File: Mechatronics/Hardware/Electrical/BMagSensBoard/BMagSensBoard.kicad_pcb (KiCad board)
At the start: 2 copper layers, 20 x 17.6 mm, 2 parts, among them J1 Conn_01x06_Male, U1 TLE5009

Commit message: Changes
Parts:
- added C27: 100nF, Encoder:C_0603_1608Metric_Pad1.05x0.95mm_HandSolder, F.Cu at (147.3, 83.7)
- renumbered J1 to J7, U1 to U7
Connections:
- net /GND renamed GND
- U7 pad 8: Net-(U1-Pad8) -> (no net)
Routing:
- net /VDD: track 9.26 -> 18.7 mm
- net /COS_P: track 10.3 -> 13.1 mm
- net GND: track 5.48 -> 6.84 mm, vias 0 -> 3
- net /COS_N: track 8.87 -> 9.61 mm
- added copper zone on F.Cu, net GND
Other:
- board size 20 x 17.6 mm -> 20 x 18.1 mm

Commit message: Changed files
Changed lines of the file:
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@@
   )
   (setup
-    (last_trace_width 0.635)
+    (last_trace_width 0.127)
     (user_trace_width 0.127)
     (user_trace_width 0.254)
@@
     (add_net GND)
   )
+  (module Encoder:SO-8_3.9x4.9mm_P1.27mm (layer F.Cu)
+    (at 146.812 88.4428)
+    (descr "SO, 8 Pin (https://www.nxp.com/docs/en/data-sheet/PCF8523.pdf), generated with kicad-footprint-generator ipc_gullwing_generator.py")
+    (tags "SO SO")
+    (attr smd)
+    (fp_text reference U7 (at -3.048 -3.4) (layer F.SilkS)
+      (effects (font (size 1 1) (thickness 0.15)))
+    )
+    (fp_text value TLE5009 (at 0 3.4) (layer F.Fab)
+      (effects (font (size 1 1) (thickness 0.15)))
+    )
+    (fp_text user %R (at 0 0) (layer F.Fab)
+      (effects (font (size 0.98 0.98) (thickness 0.15)))
+    )
+    (fp_line (start 3.7 -2.7) (end -3.7 -2.7) (layer F.CrtYd) (width 0.05))
+    (fp_line (start 3.7 2.7) (end 3.7 -2.7) (layer F.CrtYd) (width 0.05))
+    (fp_line (start -3.7 2.7) (end 3.7 2.7) (layer F.CrtYd) (width 0.05))
+    (fp_line (start -3.7 -2.7) (end -3.7 2.7) (layer F.CrtYd) (width 0.05))
+    (fp_line (start -1.95 -1.475) (end -0.975 -2.45) (layer F.Fab) (width 0.1))
+    (fp_line (start -1.95 2.45) (end -1.95 -1.475) (layer F.Fab) (width 0.1))
+    (fp_line (start 1.95 2.45) (end -1.95 2.45) (layer F.Fab) (width 0.1))
+    (fp_line (start 1.95 -2.45) (end 1.95 2.45) (layer F.Fab) (width 0.1))
+    (fp_line (start -0.975 -2.45) (end 1.95 -2.45) (layer F.Fab) (width 0.1))
+    (fp_line (start 0 -2.56) (end -3.45 -2.56) (layer F.SilkS) (width 0.12))
+    (fp_line (start 0 -2.56) (end 1.95 -2.56) (layer F.SilkS) (width 0.12))
+    (fp_line (start 0 2.56) (end -1.95 2.56) (layer F.SilkS) (width 0.12))
+    (fp_line (start 0 2.56) (end 1.95 2.56) (layer F.SilkS) (width 0.12))
+    (pad 1 smd roundrect (at -2.845 -1.905) (size 1.31 0.65) (layers F.Cu F.Paste F.Mask) (roundrect_rratio 0.25)
+      (net 3 /COS_P))
+    (pad 2 smd roundrect (at -2.845 -0.635) (size 1.31 0.6) (layers F.Cu F.Paste F.Mask) (roundrect_rratio 0.25)
+      (net 2 /COS_N))
+    (pad 3 smd roundrect (at -2.845 0.635) (size 1.31 0.6) (layers F.Cu F.Paste F.Mask) (roundrect_rratio 0.25)
+      (net 6 GND))
+    (pad 4 smd roundrect (at -2.845 1.905) (size 1.31 0.6) (layers F.Cu F.Paste F.Mask) (roundrect_rratio 0.25)
+      (net 6 GND))
+    (pad 5 smd roundrect (at 2.845 1.905) (size 1.31 0.6) (layers F.Cu F.Paste F.Mask) (roundrect_rratio 0.25)
+      (net 1 /SIN_P))
+    (pad 6 smd roundrect (at 2.845 0.635) (size 1.31 0.6) (layers F.Cu F.Paste F.Mask) (roundrect_rratio 0.25)
+      (net 5 /SIN_N))
+    (pad 7 smd roundrect (at 2.845 -0.635) (size 1.31 0.6) (layers F.Cu F.Paste F.Mask) (roundrect_rratio 0.25)
+      (net 4 /VDD))
+    (pad 8 smd roundrect (at 2.84 -1.905) (size 1.31 0.6) (layers F.Cu F.Paste F.Mask) (roundrect_rratio 0.25))
+    (model "${KIPRJMOD}/../FootPrints/3DModels/So8/User Library-so8-3.step"
+      (at (xyz 0 0 0))
+      (scale (xyz 1 1 1))
+      (rotate (xyz 0 0 0))
+    )
+  )
   (module Encoder:SolderWirePad_1x01_SMD_5x10mm (layer F.Cu)
     (at 146.812 93.7768)
@@
       (net 2 /COS_N))
   )
-  (module Encoder:SO-8_3.9x4.9mm_P1.27mm (layer F.Cu)
-    (at 146.812 88.4428)
-    (descr "SO, 8 Pin (https://www.nxp.com/docs/en/data-sheet/PCF8523.pdf), generated with kicad-footprint-generator ipc_gullwing_generator.py")
-    (tags "SO SO")
-    (attr smd)
-    (fp_text reference U7 (at -3.048 -3.4) (layer F.SilkS)
-      (effects (font (size 1 1) (thickness 0.15)))
-    )
-    (fp_text value TLE5009 (at 0 3.4) (layer F.Fab)
-      (effects (font (size 1 1) (thickness 0.15)))
-    )
-    (fp_line (start 3.7 -2.7) (end -3.7 -2.7) (layer F.CrtYd) (width 0.05))
-    (fp_line (start 3.7 2.7) (end 3.7 -2.7) (layer F.CrtYd) (width 0.05))
-    (fp_line (start -3.7 2.7) (end 3.7 2.7) (layer F.CrtYd) (width 0.05))
-    (fp_line (start -3.7 -2.7) (end -3.7 2.7) (layer F.CrtYd) (width 0.05))
-    (fp_line (start -1.95 -1.475) (end -0.975 -2.45) (layer F.Fab) (width 0.1))
-    (fp_line (start -1.95 2.45) (end -1.95 -1.475) (layer F.Fab) (width 0.1))
-    (fp_line (start 1.95 2.45) (end -1.95 2.45) (layer F.Fab) (width 0.1))
-    (fp_line (start 1.95 -2.45) (end 1.95 2.45) (layer F.Fab) (width 0.1))
-    (fp_line (start -0.975 -2.45) (end 1.95 -2.45) (layer F.Fab) (width 0.1))
-    (fp_line (start 0 -2.56) (end -3.45 -2.56) (layer F.SilkS) (width 0.12))
-    (fp_line (start 0 -2.56) (end 1.95 -2.56) (layer F.SilkS) (width 0.12))
-    (fp_line (start 0 2.56) (end -1.95 2.56) (layer F.SilkS) (width 0.12))
-    (fp_line (start 0 2.56) (end 1.95 2.56) (layer F.SilkS) (width 0.12))
-    (fp_text user %R (at 0 0) (layer F.Fab)
-      (effects (font (size 0.98 0.98) (thickness 0.15)))
-    )
-    (pad 1 smd roundrect (at -2.575 -1.905) (size 1.75 0.6) (layers F.Cu F.Paste F.Mask) (roundrect_rratio 0.25)
-      (net 3 /COS_P))
-    (pad 2 smd roundrect (at -2.575 -0.635) (size 1.75 0.6) (layers F.Cu F.Paste F.Mask) (roundrect_rratio 0.25)
-      (net 2 /COS_N))
-    (pad 3 smd roundrect (at -2.575 0.635) (size 1.75 0.6) (layers F.Cu F.Paste F.Mask) (roundrect_rratio 0.25)
-      (net 6 GND))
-    (pad 4 smd roundrect (at -2.575 1.905) (size 1.75 0.6) (layers F.Cu F.Paste F.Mask) (roundrect_rratio 0.25)
-      (net 6 GND))
-    (pad 5 smd roundrect (at 2.575 1.905) (size 1.75 0.6) (layers F.Cu F.Paste F.Mask) (roundrect_rratio 0.25)
-      (net 1 /SIN_P))
-    (pad 6 smd roundrect (at 2.575 0.635) (size 1.75 0.6) (layers F.Cu F.Paste F.Mask) (roundrect_rratio 0.25)
-      (net 5 /SIN_N))
-    (pad 7 smd roundrect (at 2.575 -0.635) (size 1.75 0.6) (layers F.Cu F.Paste F.Mask) (roundrect_rratio 0.25)
-      (net 4 /VDD))
-    (pad 8 smd roundrect (at 2.575 -1.905) (size 1.75 0.6) (layers F.Cu F.Paste F.Mask) (roundrect_rratio 0.25))
-    (model "${KIPRJMOD}/../FootPrints/3DModels/So8/User Library-so8-3.step"
-      (at (xyz 0 0 0))
-      (scale (xyz 1 1 1))
-      (rotate (xyz 0 0 0))
-    )
-  )
   (module Encoder:C_0603_1608Metric_Pad1.05x0.95mm_HandSolder (layer F.Cu)
     (at 147.32 83.7438 90)
@@
       (effects (font (size 1 1) (thickness 0.15)))
     )
+    (fp_line (start -0.8 0.4) (end -0.8 -0.4) (layer F.Fab) (width 0.1))
+    (fp_line (start -0.8 -0.4) (end 0.8 -0.4) (layer F.Fab) (width 0.1))
+    (fp_line (start 0.8 -0.4) (end 0.8 0.4) (layer F.Fab) (width 0.1))
+    (fp_line (start 0.8 0.4) (end -0.8 0.4) (layer F.Fab) (width 0.1))
+    (fp_line (start -0.171267 -0.51) (end 0.171267 -0.51) (layer F.SilkS) (width 0.12))
+    (fp_line (start -0.171267 0.51) (end 0.171267 0.51) (layer F.SilkS) (width 0.12))
+    (fp_line (start -1.65 0.73) (end -1.65 -0.73) (layer F.CrtYd) (width 0.05))
+    (fp_line (start -1.65 -0.73) (end 1.65 -0.73) (layer F.CrtYd) (width 0.05))
+    (fp_line (start 1.65 -0.73) (end 1.65 0.73) (layer F.CrtYd) (width 0.05))
     (fp_line (start 1.65 0.73) (end -1.65 0.73) (layer F.CrtYd) (width 0.05))
-    (fp_line (start 1.65 -0.73) (end 1.65 0.73) (layer F.CrtYd) (width 0.05))
-    (fp_line (start -1.65 -0.73) (end 1.65 -0.73) (layer F.CrtYd) (width 0.05))
-    (fp_line (start -1.65 0.73) (end -1.65 -0.73) (layer F.CrtYd) (width 0.05))
-    (fp_line (start -0.171267 0.51) (end 0.171267 0.51) (layer F.SilkS) (width 0.12))
-    (fp_line (start -0.171267 -0.51) (end 0.171267 -0.51) (layer F.SilkS) (width 0.12))
-    (fp_line (start 0.8 0.4) (end -0.8 0.4) (layer F.Fab) (width 0.1))
-    (fp_line (start 0.8 -0.4) (end 0.8 0.4) (layer F.Fab) (width 0.1))
-    (fp_line (start -0.8 -0.4) (end 0.8 -0.4) (layer F.Fab) (width 0.1))
-    (fp_line (start -0.8 0.4) (end -0.8 -0.4) (layer F.Fab) (width 0.1))
     (fp_text user %R (at 0 0 90) (layer F.Fab)
       (effects (font (size 0.4 0.4) (thickness 0.06)))

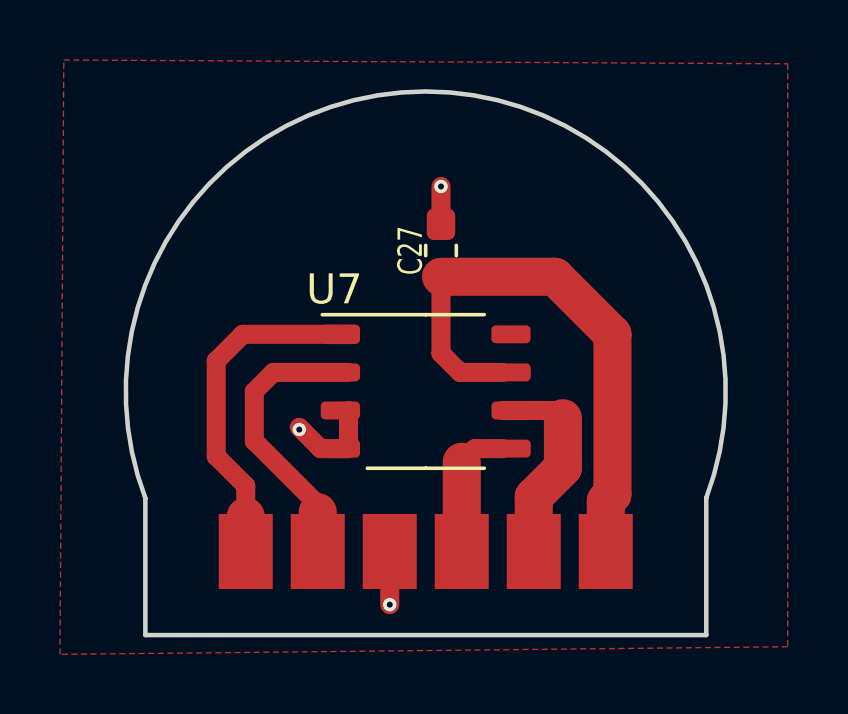
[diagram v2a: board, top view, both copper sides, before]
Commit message: Changed panelization shape
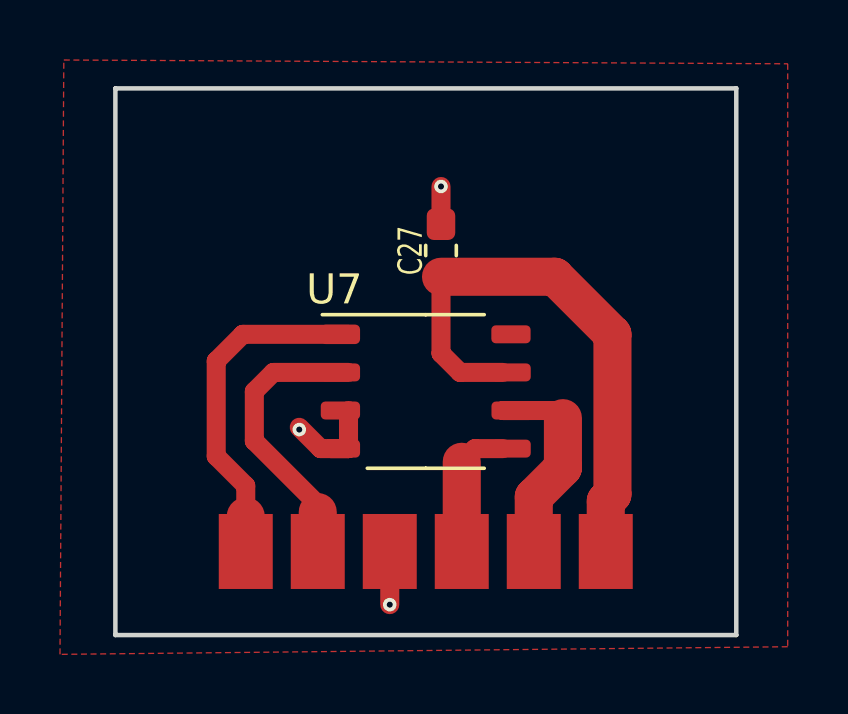
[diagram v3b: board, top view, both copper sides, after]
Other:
- board size 20 x 18.1 mm -> 20.7 x 18.2 mm
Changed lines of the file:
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@@
       (effects (font (size 1 1) (thickness 0.15)))
     )
+    (fp_line (start 0 2.56) (end 1.95 2.56) (layer F.SilkS) (width 0.12))
+    (fp_line (start 0 2.56) (end -1.95 2.56) (layer F.SilkS) (width 0.12))
+    (fp_line (start 0 -2.56) (end 1.95 -2.56) (layer F.SilkS) (width 0.12))
+    (fp_line (start 0 -2.56) (end -3.45 -2.56) (layer F.SilkS) (width 0.12))
+    (fp_line (start -0.975 -2.45) (end 1.95 -2.45) (layer F.Fab) (width 0.1))
+    (fp_line (start 1.95 -2.45) (end 1.95 2.45) (layer F.Fab) (width 0.1))
+    (fp_line (start 1.95 2.45) (end -1.95 2.45) (layer F.Fab) (width 0.1))
+    (fp_line (start -1.95 2.45) (end -1.95 -1.475) (layer F.Fab) (width 0.1))
+    (fp_line (start -1.95 -1.475) (end -0.975 -2.45) (layer F.Fab) (width 0.1))
+    (fp_line (start -3.7 -2.7) (end -3.7 2.7) (layer F.CrtYd) (width 0.05))
+    (fp_line (start -3.7 2.7) (end 3.7 2.7) (layer F.CrtYd) (width 0.05))
+    (fp_line (start 3.7 2.7) (end 3.7 -2.7) (layer F.CrtYd) (width 0.05))
+    (fp_line (start 3.7 -2.7) (end -3.7 -2.7) (layer F.CrtYd) (width 0.05))
     (fp_text user %R (at 0 0) (layer F.Fab)
       (effects (font (size 0.98 0.98) (thickness 0.15)))
     )
-    (fp_line (start 3.7 -2.7) (end -3.7 -2.7) (layer F.CrtYd) (width 0.05))
-    (fp_line (start 3.7 2.7) (end 3.7 -2.7) (layer F.CrtYd) (width 0.05))
-    (fp_line (start -3.7 2.7) (end 3.7 2.7) (layer F.CrtYd) (width 0.05))
-    (fp_line (start -3.7 -2.7) (end -3.7 2.7) (layer F.CrtYd) (width 0.05))
-    (fp_line (start -1.95 -1.475) (end -0.975 -2.45) (layer F.Fab) (width 0.1))
-    (fp_line (start -1.95 2.45) (end -1.95 -1.475) (layer F.Fab) (width 0.1))
-    (fp_line (start 1.95 2.45) (end -1.95 2.45) (layer F.Fab) (width 0.1))
-    (fp_line (start 1.95 -2.45) (end 1.95 2.45) (layer F.Fab) (width 0.1))
-    (fp_line (start -0.975 -2.45) (end 1.95 -2.45) (layer F.Fab) (width 0.1))
-    (fp_line (start 0 -2.56) (end -3.45 -2.56) (layer F.SilkS) (width 0.12))
-    (fp_line (start 0 -2.56) (end 1.95 -2.56) (layer F.SilkS) (width 0.12))
-    (fp_line (start 0 2.56) (end -1.95 2.56) (layer F.SilkS) (width 0.12))
-    (fp_line (start 0 2.56) (end 1.95 2.56) (layer F.SilkS) (width 0.12))
     (pad 1 smd roundrect (at -2.845 -1.905) (size 1.31 0.65) (layers F.Cu F.Paste F.Mask) (roundrect_rratio 0.25)
       (net 3 /COS_P))
@@
       (effects (font (size 1 1) (thickness 0.15)))
     )
+    (fp_line (start 1.65 0.73) (end -1.65 0.73) (layer F.CrtYd) (width 0.05))
+    (fp_line (start 1.65 -0.73) (end 1.65 0.73) (layer F.CrtYd) (width 0.05))
+    (fp_line (start -1.65 -0.73) (end 1.65 -0.73) (layer F.CrtYd) (width 0.05))
+    (fp_line (start -1.65 0.73) (end -1.65 -0.73) (layer F.CrtYd) (width 0.05))
+    (fp_line (start -0.171267 0.51) (end 0.171267 0.51) (layer F.SilkS) (width 0.12))
+    (fp_line (start -0.171267 -0.51) (end 0.171267 -0.51) (layer F.SilkS) (width 0.12))
+    (fp_line (start 0.8 0.4) (end -0.8 0.4) (layer F.Fab) (width 0.1))
+    (fp_line (start 0.8 -0.4) (end 0.8 0.4) (layer F.Fab) (width 0.1))
+    (fp_line (start -0.8 -0.4) (end 0.8 -0.4) (layer F.Fab) (width 0.1))
     (fp_line (start -0.8 0.4) (end -0.8 -0.4) (layer F.Fab) (width 0.1))
-    (fp_line (start -0.8 -0.4) (end 0.8 -0.4) (layer F.Fab) (width 0.1))
-    (fp_line (start 0.8 -0.4) (end 0.8 0.4) (layer F.Fab) (width 0.1))
-    (fp_line (start 0.8 0.4) (end -0.8 0.4) (layer F.Fab) (width 0.1))
-    (fp_line (start -0.171267 -0.51) (end 0.171267 -0.51) (layer F.SilkS) (width 0.12))
-    (fp_line (start -0.171267 0.51) (end 0.171267 0.51) (layer F.SilkS) (width 0.12))
-    (fp_line (start -1.65 0.73) (end -1.65 -0.73) (layer F.CrtYd) (width 0.05))
-    (fp_line (start -1.65 -0.73) (end 1.65 -0.73) (layer F.CrtYd) (width 0.05))
-    (fp_line (start 1.65 -0.73) (end 1.65 0.73) (layer F.CrtYd) (width 0.05))
-    (fp_line (start 1.65 0.73) (end -1.65 0.73) (layer F.CrtYd) (width 0.05))
     (fp_text user %R (at 0 0 90) (layer F.Fab)
       (effects (font (size 0.4 0.4) (thickness 0.06)))
@@
     )
   )
-  (gr_line (start 136.466 96.064) (end 157.162639 96.064) (layer Dwgs.User) (width 0.15))
-  (gr_line (start 157.162639 92) (end 157.162639 96.0628) (layer Dwgs.User) (width 0.15))
-  (gr_line (start 155.162639 92) (end 155.162639 96.0628) (layer Dwgs.User) (width 0.15))
-  (gr_line (start 136.466 92) (end 136.466 96.0628) (layer Dwgs.User) (width 0.15))
-  (gr_line (start 138.466 92) (end 138.466 96.0628) (layer Dwgs.User) (width 0.15))
-  (gr_line (start 156.162639 91.987787) (end 156.162639 96.5628) (layer Edge.Cuts) (width 0.15))
-  (gr_line (start 137.466 96.5628) (end 156.162639 96.5628) (layer Edge.Cuts) (width 0.15))
-  (gr_line (start 137.466 92) (end 137.466 96.5628) (layer Edge.Cuts) (width 0.15))
+  (gr_line (start 136.466 78.34) (end 157.162639 78.34) (layer Edge.Cuts) (width 0.15))
+  (gr_line (start 136.466 96.5628) (end 157.162639 96.5628) (layer Edge.Cuts) (width 0.15))
+  (gr_line (start 157.162639 78.34) (end 157.162639 96.5628) (layer Edge.Cuts) (width 0.15))
+  (gr_line (start 155.162639 92) (end 155.162639 96.5628) (layer Dwgs.User) (width 0.15))
+  (gr_line (start 136.466 78.34) (end 136.466 96.5628) (layer Edge.Cuts) (width 0.15))
+  (gr_line (start 138.466 92) (end 138.466 96.5628) (layer Dwgs.User) (width 0.15))
+  (gr_line (start 156.162639 91.987787) (end 156.162639 96.5628) (layer Dwgs.User) (width 0.15))
+  (gr_line (start 137.466 92) (end 137.466 96.5628) (layer Dwgs.User) (width 0.15))
   (gr_circle (center 146.812 88.4428) (end 154.812 88.4428) (layer Dwgs.User) (width 0.15))
   (gr_line (start 136.466 92) (end 157.162639 92) (layer Dwgs.User) (width 0.15))
-  (gr_arc (start 146.812 88.4428) (end 137.466 92) (angle 221.6) (layer Edge.Cuts) (width 0.15))
+  (gr_arc (start 146.812 88.4428) (end 137.466 92) (angle 221.6) (layer Dwgs.User) (width 0.15))
   (segment (start 148.45 90.3478) (end 149.387 90.3478) (width 0.635) (layer F.Cu) (net 1))
   (segment (start 148.012 90.7858) (end 148.45 90.3478) (width 0.635) (layer F.Cu) (net 1))
